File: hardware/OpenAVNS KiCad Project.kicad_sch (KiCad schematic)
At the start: 214 parts, among them J1 Conn_ARM_JTAG_SWD_10, J2 AudioPlug3, J3 USB_C_Receptacle, J4 Conn_01x02_Pin, J5 Conn_01x03_Pin, Q1 BCV62, Q2 BC847, Q3 BC857, Q4 BCV61, Q5 BCV62, Q6 BC847, Q7 BC857, Q8 BCV61, SW1 SW_SPDT, T1 Wurth 750315839 - 1:10, 40uH, U1 TS5A3159AYZPR, U10 TLV9062, U11 LIS2DH12, U12 OPA455, U13 74AUC1G74, U14 TPS61200DRC, U15 LT1615ES5_TRPBF, U16 LT8304IS8E_PBF, U17 MCP73831-2-OT, U2 TLV9004xRUCR, U3 MCP4725xxx-xCH, U4 TS5A3159AYZPR, U5 nRF52840, U6 TS5A3159AYZPR, U7 MCP4725xxx-xCH, U8 TS5A3159AYZPR, U9 OPA455, Y1 32MHz - X322532MOB4SI

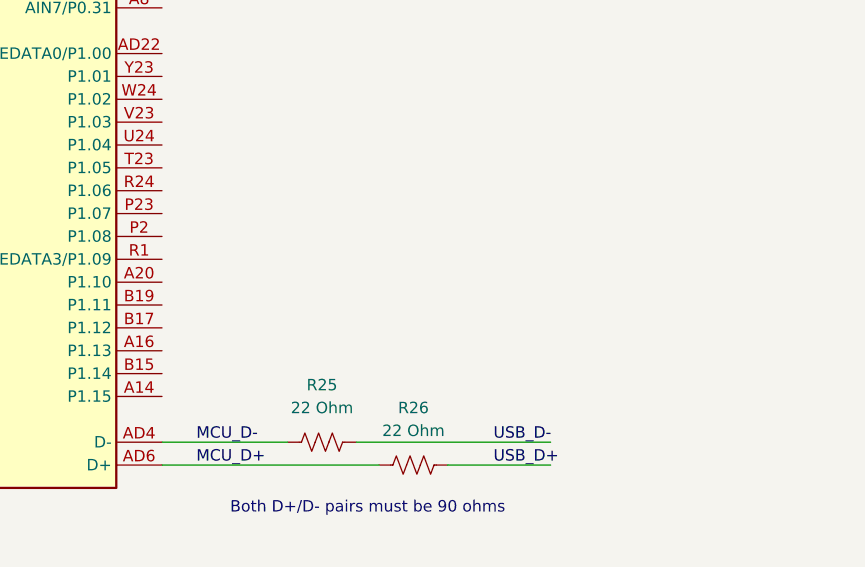
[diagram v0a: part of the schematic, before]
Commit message: Added GPIO pin for triggering or other multipurpose applications
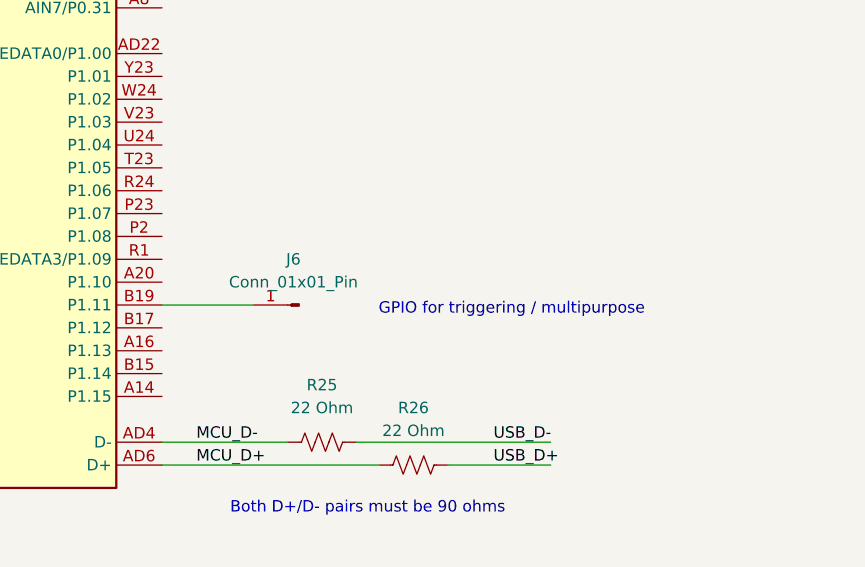
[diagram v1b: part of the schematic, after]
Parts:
- added J6: Conn_01x01_Pin, Connector_PinHeader_1.00mm:PinHeader_1x01_P1.00mm_Horizontal, symbol Connector:Conn_01x01_Pin
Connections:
- net at U5.B19 (P1.11): now also J6.1 (Pin_1)
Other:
- note added: "GPIO for triggering / multipurpose"
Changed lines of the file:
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@@
 		)
 	)
+	(text "GPIO for triggering / multipurpose"
+		(exclude_from_sim no)
+		(at 217.932 210.058 0)
+		(effects
+			(font
+				(size 1.27 1.27)
+			)
+		)
+	)
 	(text "D+ / D- differential pair must be 90 Ohms"
 		(exclude_from_sim no)
@@
 	(wire
 		(pts
+			(xy 179.07 209.55) (xy 189.23 209.55)
+		)
+		(stroke
+			(width 0)
+			(type default)
+		)
+	)
+	(wire
+		(pts
 			(xy 538.48 67.31) (xy 556.26 67.31)
 		)
@@
 					(unit 1)
 				)
+			)
+		)
+	)
+	(symbol
+		(lib_id "Connector:Conn_01x01_Pin")
+		(at 194.31 209.55 180)
+		(unit 1)
+		(exclude_from_sim no)
+		(in_bom yes)
+		(on_board yes)
+		(dnp no)
+		(fields_autoplaced yes)
+		(property "Reference" "J6"
+			(at 193.675 204.47 0)
+			(effects
+				(font
+					(size 1.27 1.27)
+				)
+			)
+		)
+		(property "Value" "Conn_01x01_Pin"
+			(at 193.675 207.01 0)
+			(effects
+				(font
+					(size 1.27 1.27)
+				)
+			)
+		)
+		(property "Footprint" "Connector_PinHeader_1.00mm:PinHeader_1x01_P1.00mm_Horizontal"
+			(at 194.31 209.55 0)
+			(effects
+				(font
+					(size 1.27 1.27)
+				)
+				(hide yes)
+			)
+		)
+		(property "Datasheet" "~"
+			(at 194.31 209.55 0)
+			(effects
+				(font
+					(size 1.27 1.27)
+				)
+				(hide yes)
+			)
+		)
+		(property "Description" "Generic connector, single row, 01x01, script generated"
+			(at 194.31 209.55 0)
+			(effects
+				(font
+					(size 1.27 1.27)
+				)
+				(hide yes)
+			)
+		)
+		(pin "1"
+		)
+		(instances
+			(project ""
+				(path "/0fd1d23b-f00b-4e4e-bb2e-2a3aca0605f8"
+					(reference "J6")
+					(unit 1)
+				)

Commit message: Edited based on Maros advice, thanks
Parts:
- R15: value R_US -> 1k
- R16: value R_US -> 150 Ohm
- R29: value R_US -> 100 Ohm
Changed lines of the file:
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@@
 			)
 		)
-		(property "Value" "R_US"
+		(property "Value" "100 Ohm"
 			(at 480.06 241.3 90)
 			(effects
@@
 			)
 		)
-		(property "Value" "R_US"
+		(property "Value" "150 Ohm"
 			(at 521.97 153.6699 0)
 			(effects
@@
 			)
 		)
-		(property "Value" "R_US"
+		(property "Value" "1k"
 			(at 511.81 153.6699 0)
 			(effects

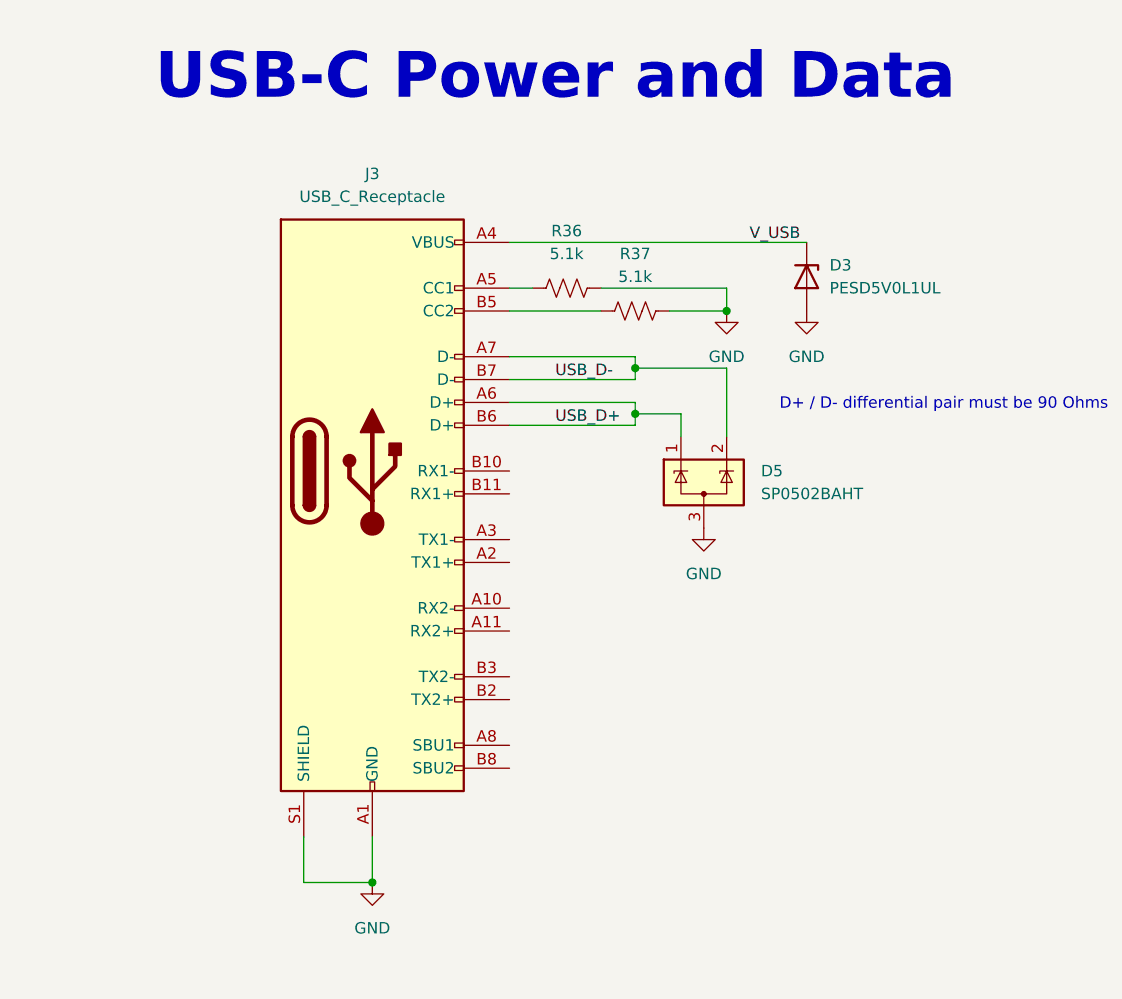
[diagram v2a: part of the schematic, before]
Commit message: Updated USB connector and routing
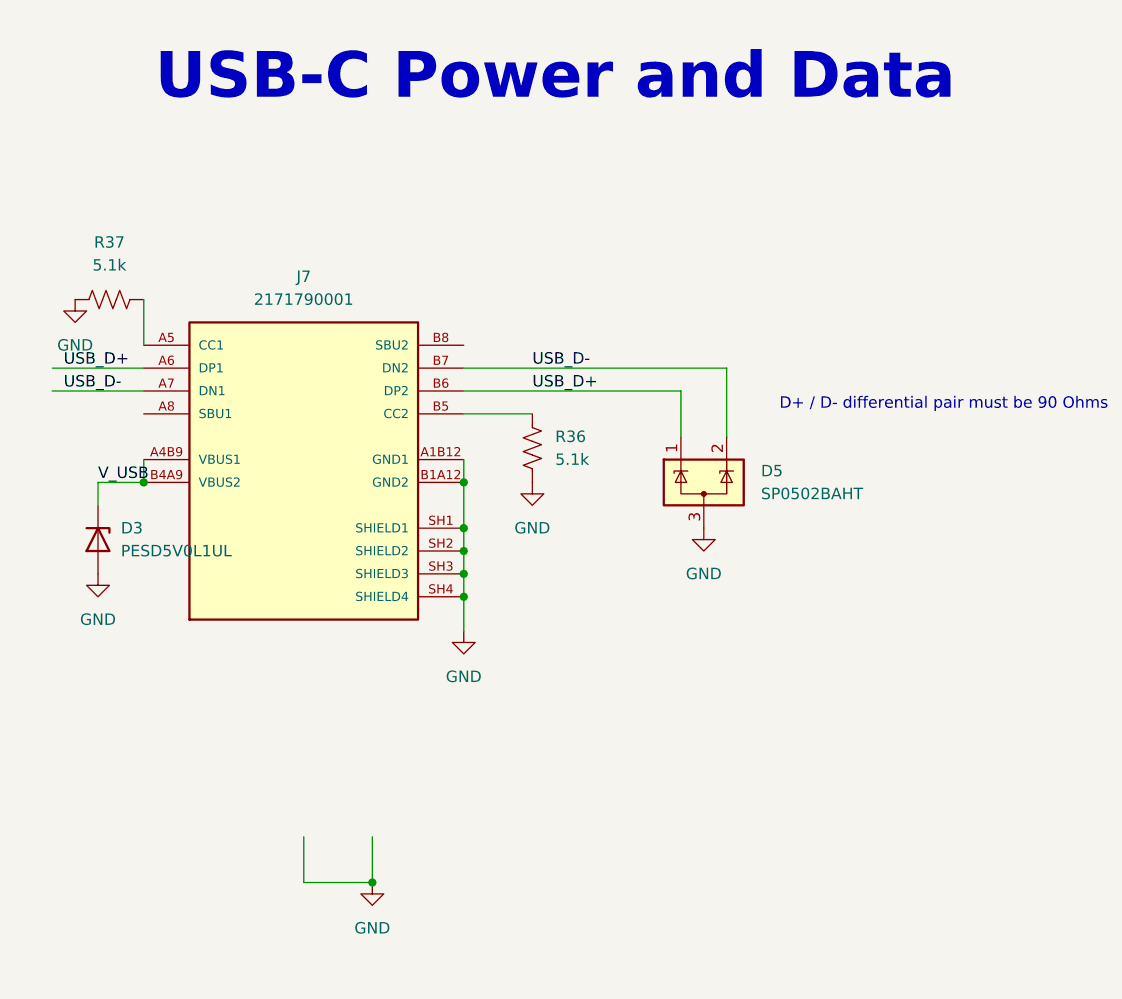
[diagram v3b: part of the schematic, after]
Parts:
- removed J3: USB_C_Receptacle, Connector_USB:USB_C_Receptacle_Amphenol_12401548E4-2A, symbol Connector:USB_C_Receptacle
- added J7: 2171790001, Footprints:MOLEX_2171790001, symbol 2171790001:2171790001
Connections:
- net GND: now also R36.2, R37.2, J7.A1B12 (GND1), J7.B1A12 (GND2), J7.SH1 (SHIELD1), J7.SH2 (SHIELD2), J7.SH3 (SHIELD3), J7.SH4 (SHIELD4); no longer R36.1, R37.1
- net USB_D+: now also J7.A6 (DP1), J7.B6 (DP2)
- net USB_D-: now also J7.A7 (DN1), J7.B7 (DN2)
- net V_USB: now also J7.A4B9 (VBUS1), J7.B4A9 (VBUS2)
- new net: J7.B5 (CC2), R36.1
- new net: J7.A5 (CC1), R37.1
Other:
- moved on the sheet: D3, R36, R37

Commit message: Replaced zero ohm resistors with headers
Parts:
- removed R49, R52, R53, R54, R55, R60: 0 Ohm, Resistor_SMD:R_0603_1608Metric_Pad0.98x0.95mm_HandSolder, symbol Device:R_US
- added J3, J8, J9: Conn_02x02_Top_Bottom, Connector_PinSocket_2.54mm:PinSocket_2x02_P2.54mm_Vertical, symbol Connector_Generic:Conn_02x02_Top_Bottom
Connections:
- net +20V: now also J8.2 (Pin_2)
- net +50V: now also J8.1 (Pin_1)
- net +HV: now also J8.3 (Pin_3), J8.4 (Pin_4)
- net -20V: now also J9.2 (Pin_2)
- net -50V: now also J9.1 (Pin_1)
- net -HV: now also J9.3 (Pin_3), J9.4 (Pin_4)
- net 20V_ON: now also J3.4 (Pin_4)
- net 50V_ON: now also J3.3 (Pin_3)
- net HV_ON: now also J3.1 (Pin_1), J3.2 (Pin_2)
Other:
- moved on the sheet: TP32

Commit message: Updated footprint of switches based on component availability
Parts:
- removed TP24: TestPoint, TestPoint:TestPoint_Pad_D2.0mm, symbol Connector:TestPoint
- removed U1, U4, U6, U8: TS5A3159AYZPR, Package_BGA:Texas_DSBGA-6_0.9x1.4mm_Layout2x3_P0.5mm, symbol Analog_Switch:TS5A3159AYZPR
- added U18, U19, U20, U21: TS5A3159DCKR, Footprints:SOT65P210X110-6N, symbol TS5A3159DCKR:TS5A3159DCKR
- C15, C16: value 22uF, 100V -> 22uF
- C35, C45: value 22uF, 100V -> 22uF, 25V
- C42: value 22uF, 50V -> 22uF, 6.3V
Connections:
- net +3.3V: now also U18.5, U19.5, U20.5, U21.5
- net C1A_ON: now also U18.6
- net C1C_ON: now also U19.6
- net C2A_ON: now also U20.6
- net C2C_ON: now also U21.6
- net GND: now also U18.2, U19.2, U20.2, U21.2
- net at TP16.1, U7.1 (VOUT): now also U20.4, U21.4
- net at TP3.1, U3.1 (VOUT): now also U18.4, U19.4
- net at R30.1, U2.11 (+): now also U21.3
- net at R9.1, U2.4 (+): now also U19.3
- net at R23.2, U2.9 (+): now also U20.3
- net at R4.2, U2.2 (+): now also U18.3
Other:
- moved on the sheet: C2, C22, C24, C9

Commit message: Updated U13 footprint
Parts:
- U13: footprint Package_SO:SSOP-8_2.95x2.8mm_P0.65mm -> Package_DFN_QFN:Texas_UQFN-8_1.5x1.5mm_P0.5mm
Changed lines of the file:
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@@
 			)
 		)
-		(property "Footprint" "Package_SO:SSOP-8_2.95x2.8mm_P0.65mm"
+		(property "Footprint" "Package_DFN_QFN:Texas_UQFN-8_1.5x1.5mm_P0.5mm"
 			(at 661.67 378.46 0)
 			(effects
